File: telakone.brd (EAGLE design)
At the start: 100 x 100 mm, 124 parts, among them X2 MPT0.5/8-2.54, X3 MPT0.5/8-2.54, X4 PIIKKIRIMA-2, X5 PIIKKIRIMA-5, X7 U.FL-R-SMT-1, X8 MPT0.5/8-2.54, X9 629105136821

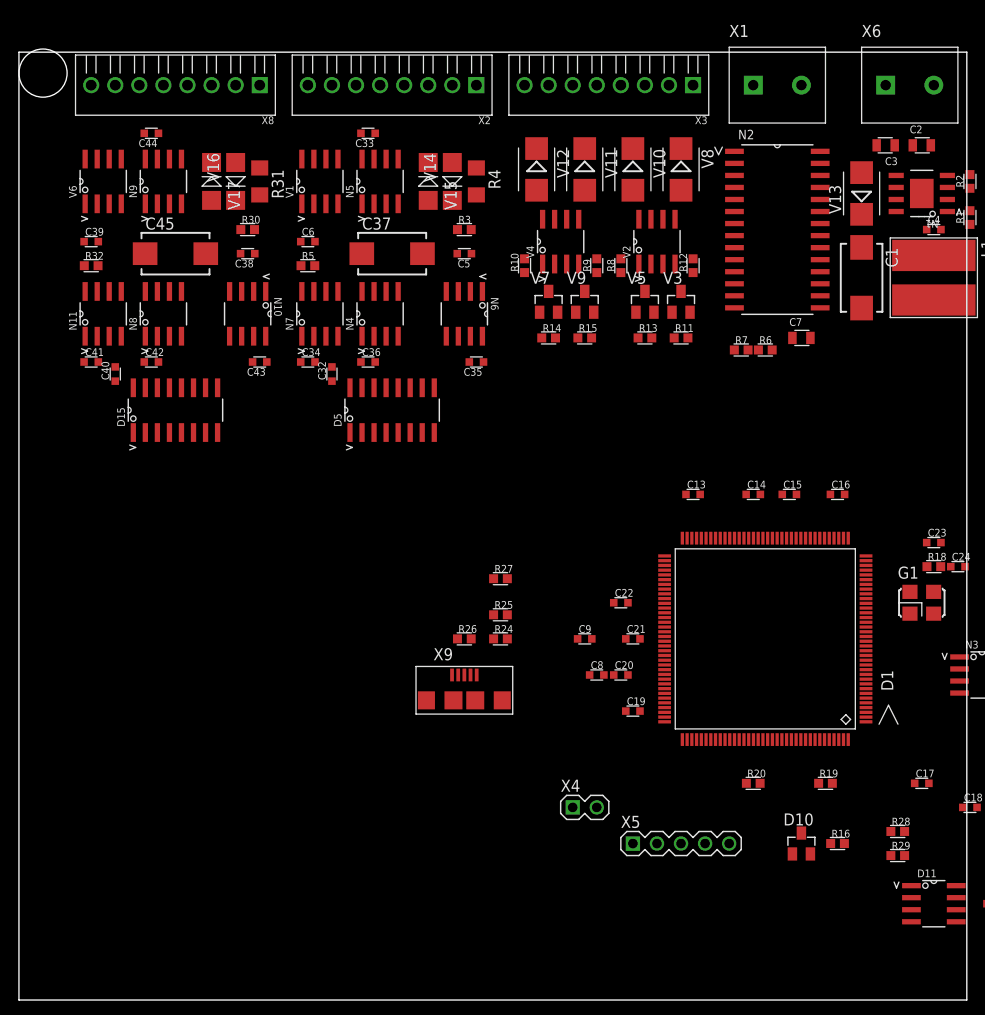
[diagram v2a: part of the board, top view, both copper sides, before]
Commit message: joystick inputs, change motor driver to plain fets, motor current measurement
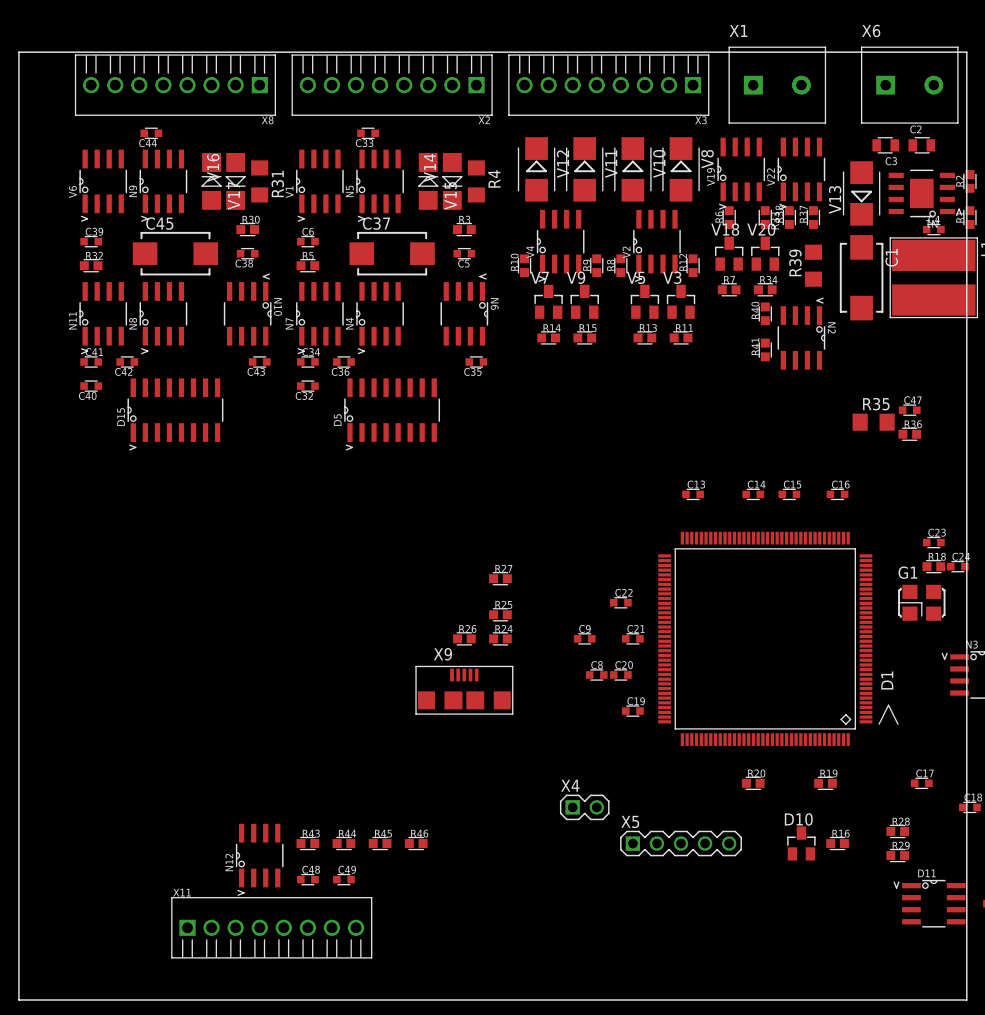
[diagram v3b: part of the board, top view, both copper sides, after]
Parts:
- removed C7: (no value), omat_ic_2:C0805
- added C47, C48, C49: (no value), omat_ic_2:C0603
- added N12: TS921IDT, omat_ic_2:SOIC8-N_MC
- added R33, R34, R37, R38, R43, R44, R45, R46: (no value), omat_ic_2:R0603
- added R35: 5k90, omat_ic_2:R1206
- added R36: 825, omat_ic_2:R0603
- added R39: ERJ-8BWFR010V, omat_ic_2:R1206
- added R40: 10, omat_ic_2:R0603
- added R41: 499, omat_ic_2:R0603
- added V18, V20: 2N7002K, omat_ic_2:SOT23
- added V19: AO4803A, omat_ic_2:SOIC8-N_MC
- added V22: AO4886, omat_ic_2:SOIC8-N_MC
- added X11: MPT0.5/8-2.54, omat_ic_2:MPT0.5/8-2.54
- N2: value BTM7710G -> LTC2050CS8; device omat_ic_2:SOIC28-W_MC -> omat_ic_2:SOIC8-N_MC
- moved R6 14.5 mm to (74.9, 82.5), turned to 90 degrees
- moved N2 11.7 mm to (82.5, 69.8), turned to 270 degrees
- moved R7 6.48 mm to (74.9, 74.9)
- moved C32 2.84 mm to (30.5, 64.8), turned to 180 degrees
- moved C40 2.84 mm to (7.62, 64.8), turned to 180 degrees
- moved C42 2.54 mm to (11.4, 67.3), turned to 180 degrees
- moved C36 2.54 mm to (34.3, 67.3), turned to 180 degrees
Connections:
- net I2CSCL renamed I2C1SCL
- net I2CSDA renamed I2C1SDA
- net N$22 renamed VCAP2
- net N$23 renamed VCAP1
- net N$25 renamed VDDA
- removed net N$16: R15.1, V9.1
- removed net N$8: N2.13, N2.7, R7.2
- new net BUTTON1: D1.11, R45.1, X11.1
- new net BUTTON2: D1.12, R46.1, X11.2
- new net D1BRAKE: D1.69, D5.5
- new net D1REVERSE: D1.70, D5.6
- new net D1SPICLK: D1.74, D5.3
- new net D1SPICSL: D1.73, D5.2
- new net D1SPIMISO: D1.75, D5.7
- new net D1SPIMOSI: D1.76, D5.4
- new net D2BRAKE: D1.97, D15.5
- new net D2REVERSE: D1.98, D15.6
- new net D2SPICLK: D1.111
- new net D2SPICSL: D1.99, D15.2
- new net D2SPIMISO: D1.112, D15.7
- new net D2SPIMOSI: D1.113, D15.4
- new net DSPICLK: D15.3
- new net MEAS12V: C47.1, D1.34, R35.2, R36.2
- new net MOTOR_CURR: D1.13, N2.6, R41.1
- new net MOTOR_H1: D1.4, R7.1, V18.1
- new net MOTOR_H2: D1.5, R34.1, V20.1
- new net MOTOR_L1: D1.2, R37.1, V22.4
- new net MOTOR_L2: D1.3, R38.1, V22.2
- new net NERT4: V19.7, V19.8, V22.5, V22.6, X1.1
- new net NERT5: V19.5, V19.6, V22.7, V22.8, X1.2
- new net OUT1: D1.18, R11.1, V3.1
- new net OUT2: D1.19, R13.1, V5.1
- new net OUT3: D1.20, R14.1, V7.1
- new net OUT4: D1.21, R15.1, V9.1
- new net POT1: C49.1, D1.14, R43.1
- new net POT2: C48.1, D1.15, R44.1
- net +12V: now also R33.2, R35.1, R6.2, V19.1, V19.3; no longer C7.1, N2.10, N2.19, N2.24, N2.5
- net +3V3: now also N12.7, N2.1, N2.7, R45.2, R46.2
- net GND: now also C47.2, C48.2, C49.2, N12.4, N2.4, R34.2, R36.1, R39.1, R40.2, R7.2, V18.2, V20.2, X11.5, X11.8; no longer C7.2, N2.16, N2.17, N2.26, N2.27, N2.6, R6.1, R7.1
- net N$12: now also R43.2, X11.4; no longer R13.1, V5.1
- net N$14: now also R44.2, X11.7; no longer R14.1, V7.1
- net N$3: now also R6.1, V18.3, V19.2; no longer N2.12, N2.14, N2.15, N2.18, N2.20, N2.21, X1.1
- net N$5: now also N12.2, N12.6, X11.3, X11.6; no longer N2.1, N2.22, N2.23, N2.25, N2.28, N2.3, X1.2
- net N$6: now also R33.1, V19.4, V20.3; no longer R11.1, V3.1
- net N$7: now also N2.3, R37.2, R38.2, R39.2, V22.1, V22.3; no longer N2.8
- net N$9: now also R40.1, R41.2; no longer N2.9, R6.2
- net VREF25: now also N12.3

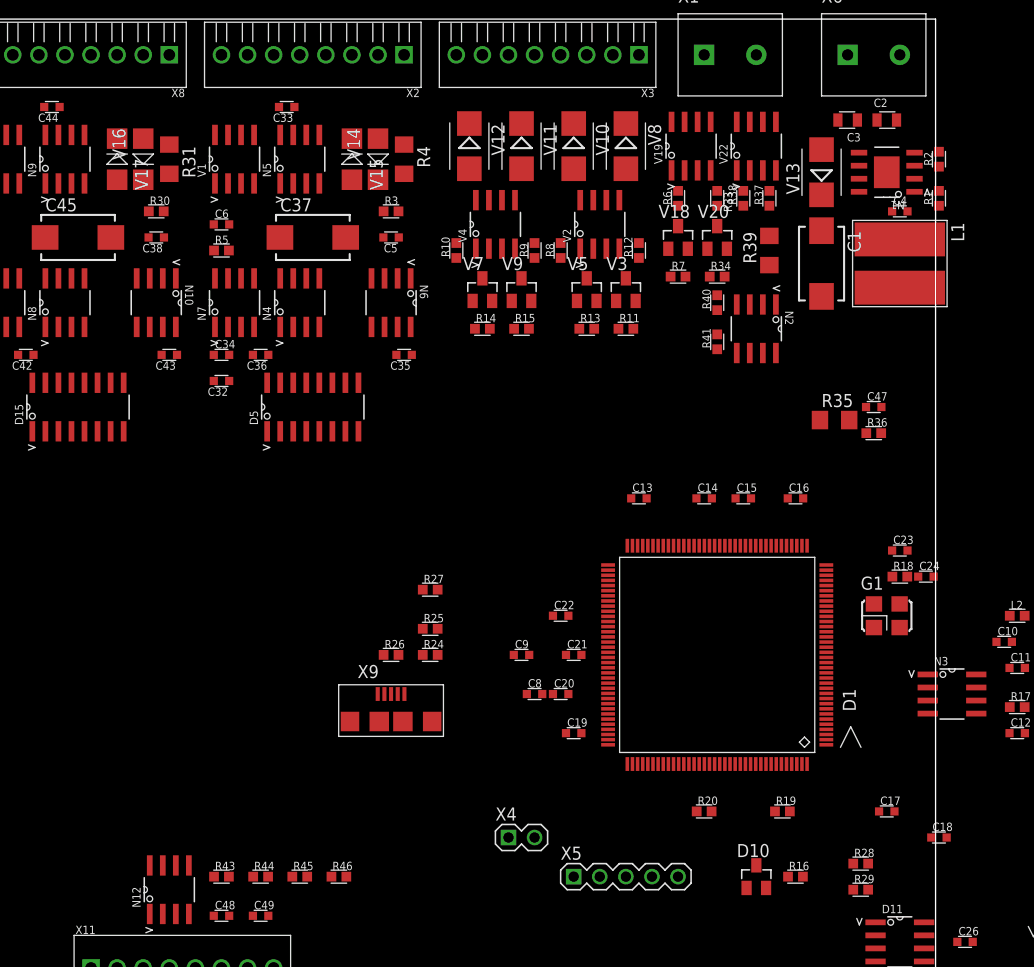
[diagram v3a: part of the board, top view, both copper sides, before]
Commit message: add some protection
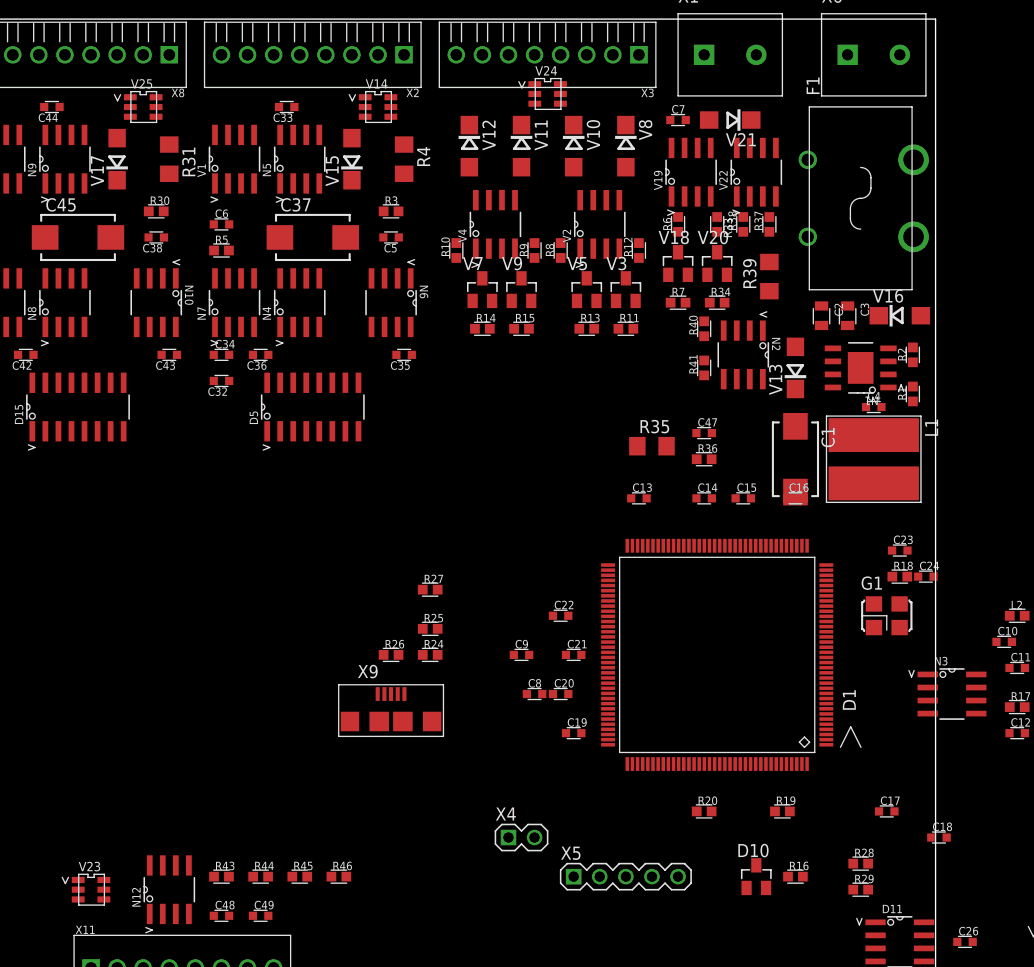
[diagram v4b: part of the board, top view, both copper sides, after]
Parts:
- added C7: (no value), omat_ic_2:C0603
- added F1: KEYSTONE-3549-2, omat_ic_2:KEYSTONE-3549-2
- added V21: SMAJXXCA, omat_ic_2:DO214AC
- added V23: WURTH 82402304, omat_ic_2:SOT23-6
- added V24: ESDA19SC6, omat_ic_2:SOT23-6
- added V25: ESDAXXSC6, omat_ic_2:SOT23-6
- V10, V11, V12, V13, V8: value SK34B -> SK34A; device diode:SMB -> omat_ic_2:DO214AC
- V14: value 1SMA5.0AT -> ESDAXXSC6; device EKE:403D-2 -> omat_ic_2:SOT23-6
- V15, V17: value 1SMA5.0AT -> SMAJ5.0A; device EKE:403D-2 -> omat_ic_2:DO214AC
- V16: value 1SMA5.0AT -> SMAJXXA; device EKE:403D-2 -> omat_ic_2:DO214AC
- moved V16 75.2 mm to (96.5, 71.1), turned to 0 degrees
- moved C2 20.1 mm to (88.9, 71.1), turned to 270 degrees
- moved C1 19.2 mm to (86.4, 57.1)
- moved C4 19.2 mm to (94.0, 62.2)
- moved L1 19.2 mm to (94.0, 57.1)
- moved N1 19.2 mm to (92.7, 66.0)
- moved V13 19.2 mm to (86.4, 66.0)
- moved R1 19.2 mm to (97.8, 63.5)
- moved R2 19.2 mm to (97.8, 67.3)
- moved C3 19.0 mm to (91.4, 71.1), turned to 270 degrees
- moved R35 18.0 mm to (72.4, 58.4)
- moved C47 16.7 mm to (77.5, 59.7)
- moved R36 16.7 mm to (77.5, 57.1)
- moved V14 5.08 mm to (45.7, 91.4), turned to 0 degrees
- moved R40 2.84 mm to (77.5, 69.8)
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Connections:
- new net N$8: F1.2, F1.3, X6.1
- net +12V: now also F1.1, F1.4, V16.C; no longer X6.1
- net AIN_1: now also V14.6; no longer V14.P$2
- net AIN_2: now also V25.6; no longer V16.P$2
- net BRAKE_OD_1: now also V14.3
- net BRAKE_OD_2: now also V25.3
- net BUTTON1: now also V23.1
- net BUTTON2: now also V23.3
- net GND: now also V16.A, V23.2, V23.5, V24.2, V24.5
- net N$17: now also V24.6
- net N$19: now also V24.4
- net N$20: now also V24.3
- net N$21: now also V24.1
- net NERT4: now also C7.1, V21.A
- net NERT5: now also C7.2, V21.C
- net POT1: now also V23.4
- net POT2: now also V23.6
- net REVERSE_OD_1: now also V14.1
- net REVERSE_OD_2: now also V25.1
- net THROTTLE_BUFFERED_1: now also V14.4
- net THROTTLE_BUFFERED_2: now also V25.4
- net V+1: now also V15.C; no longer V15.P$2
- net V+2: now also V17.C; no longer V17.P$2
- net V-1: now also V14.2, V14.5, V15.A; no longer V14.P$1, V15.P$1
- net V-2: now also V17.A, V25.2, V25.5; no longer V16.P$1, V17.P$1

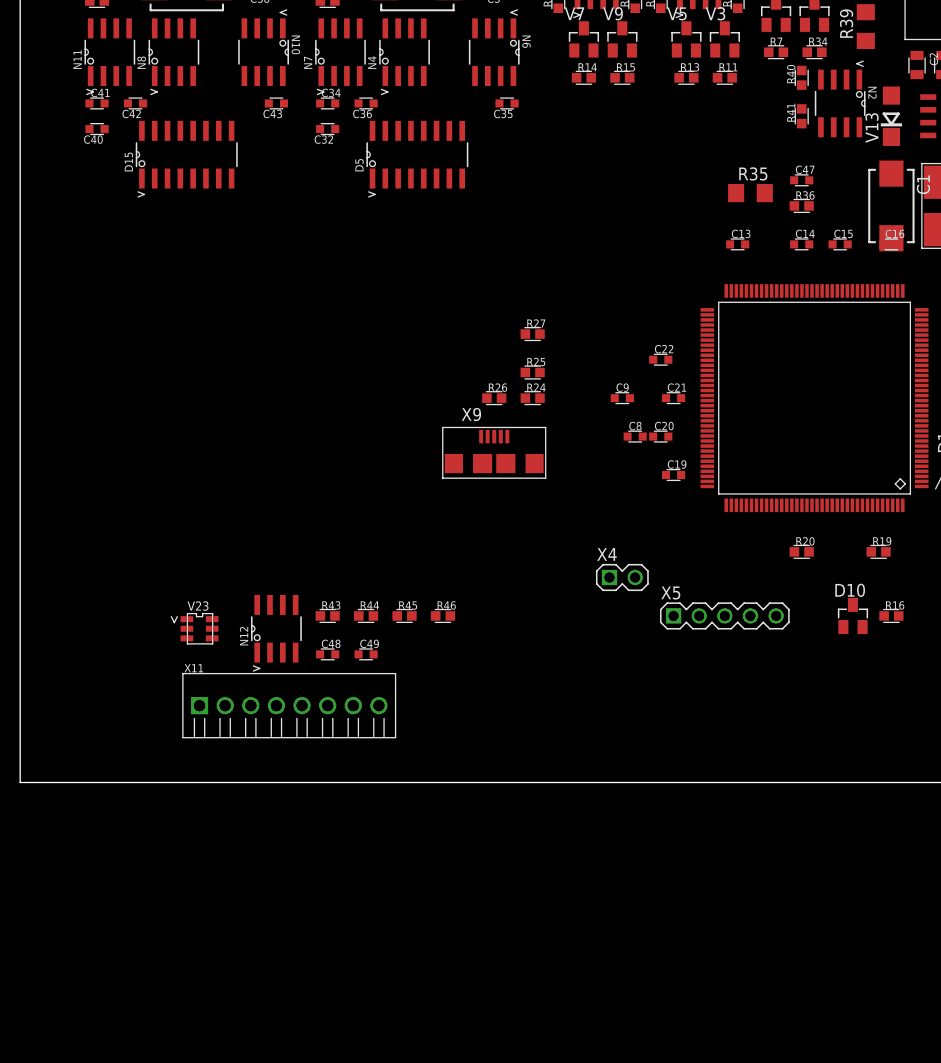
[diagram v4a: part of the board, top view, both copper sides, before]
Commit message: Schematics tuning
Series resistors to SWDIO/SWCLK
Pulldown to DAC outputs (HighZ after powerup)
Some missing values added
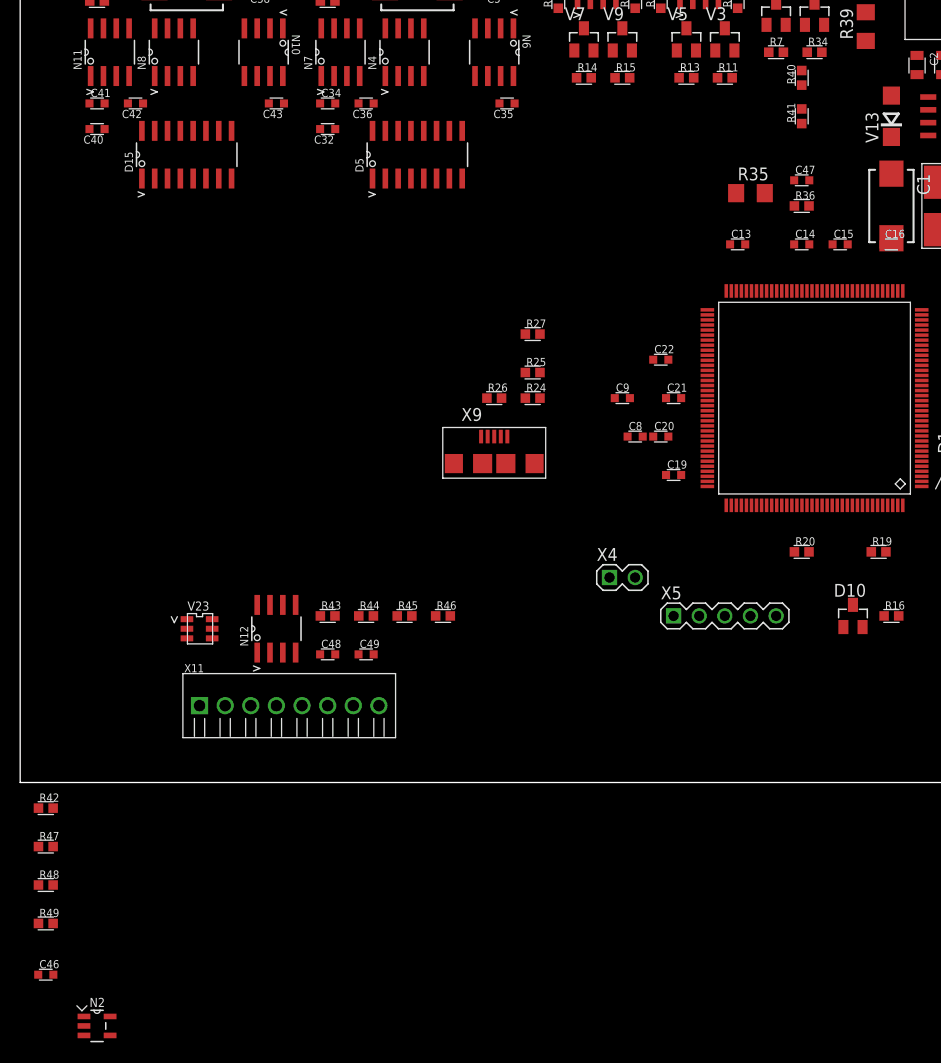
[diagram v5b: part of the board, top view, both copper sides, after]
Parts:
- added C46: (no value), omat_ic_2:C0603
- added R42, R47: (no value), omat_ic_2:R0603
- added R48, R49: 100k, omat_ic_2:R0603
- C10, C13, C14, C15, C16, C17, C18, C19, C20, C21, C22, C26, C27, C31, C32, C33, C34, C35, C36, C40, C41, C42, C43, C44: value (none) -> 100n
- C11, C12, C28, C29, C30, C39, C6: value (none) -> 2u2
- N2: value LTC2050CS8 -> LTC2050CS5; device omat_ic_2:SOIC8-N_MC -> omat_ic_2:SOT95P280X145-5N
- R17, R32, R5: value (none) -> 1k
- moved N2 117.4 mm to (7.62, -24.1), turned to 0 degrees
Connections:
- new net N$16: D1.109, R47.2
- new net N$22: D1.105, R42.2
- net +3V3: now also C46.1, N2.5; no longer N2.1, N2.7
- net GND: now also C46.2, N2.2; no longer N2.4
- net MOTOR_CURR: now also N2.1; no longer N2.6
- net N$9: now also N2.4; no longer N2.2
- net SWCLK: now also R47.1; no longer D1.109
- net SWDIO: now also R42.1; no longer D1.105
- net THROTTLE_1: now also R49.2
- net THROTTLE_2: now also R48.2
- net V-1: now also R49.1
- net V-2: now also R48.1
